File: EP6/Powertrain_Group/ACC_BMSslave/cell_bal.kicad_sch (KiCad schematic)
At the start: 6 parts, among them IC13 NX2301P,215

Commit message: ACC_BMSslave pcb priliminary layout
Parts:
- D13: footprint LED_SMD:LED_0805_2012Metric -> LED_SMD:LED_0603_1608Metric
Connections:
- net CT-: now also D13.1 (K); no longer R103.2
- net at R103.1: now also IC13.3 (D), R104.2, R105.2; no longer D13.1 (K)
- new net: D13.2 (A), R103.2
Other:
- moved on the sheet: D13, R103
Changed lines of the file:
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@@
 	(wire
 		(pts
-			(xy 87.63 76.2) (xy 87.63 77.47)
+			(xy 87.63 73.66) (xy 87.63 74.93)
 		)
 		(stroke
@@
 	(symbol
 		(lib_id "Device:R_Small")
-		(at 87.63 80.01 0)
+		(at 87.63 71.12 0)
 		(unit 1)
 		(exclude_from_sim no)
@@
 		(fields_autoplaced yes)
 		(property "Reference" "R103"
-			(at 90.17 78.7399 0)
+			(at 90.17 69.8499 0)
 			(effects
 				(font
@@
 		)
 		(property "Value" "510"
-			(at 90.17 81.2799 0)
+			(at 90.17 72.3899 0)
 			(effects
 				(font
@@
 		)
 		(property "Footprint" "Resistor_SMD:R_0402_1005Metric"
-			(at 87.63 80.01 0)
+			(at 87.63 71.12 0)
 			(effects
 				(font
@@
 		)
 		(property "Datasheet" "~"
-			(at 87.63 80.01 0)
+			(at 87.63 71.12 0)
 			(effects
 				(font
@@
 		)
 		(property "Description" "Resistor, small symbol"
-			(at 87.63 80.01 0)
+			(at 87.63 71.12 0)
 			(effects
 				(font
@@
 	(symbol
 		(lib_id "Device:LED")
-		(at 87.63 72.39 90)
+		(at 87.63 78.74 90)
 		(unit 1)
 		(exclude_from_sim no)
@@
 		(fields_autoplaced yes)
 		(property "Reference" "D13"
-			(at 91.44 72.7074 90)
+			(at 91.44 79.0574 90)
 			(effects
 				(font
@@
 		)
 		(property "Value" "RED"
-			(at 91.44 75.2474 90)
+			(at 91.44 81.5974 90)
 			(effects
 				(font
@@
 			)
 		)
-		(property "Footprint" "LED_SMD:LED_0805_2012Metric"
-			(at 87.63 72.39 0)
+		(property "Footprint" "LED_SMD:LED_0603_1608Metric"
+			(at 87.63 78.74 0)
 			(effects
 				(font
@@
 		)
 		(property "Datasheet" "~"
-			(at 87.63 72.39 0)
+			(at 87.63 78.74 0)
 			(effects
 				(font
@@
 		)
 		(property "Description" "Light emitting diode"
-			(at 87.63 72.39 0)
-			(effects
-				(font
+			(at 87.63 78.74 0)
+			(effects
+				(font

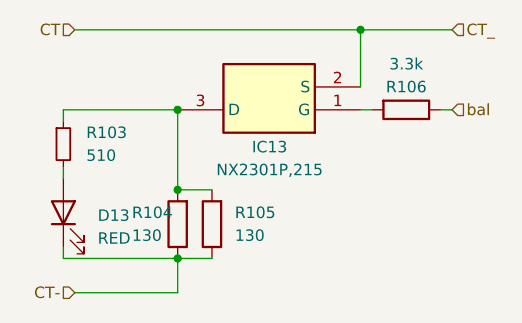
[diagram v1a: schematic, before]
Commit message: ACC_BMSslave changed balancing current
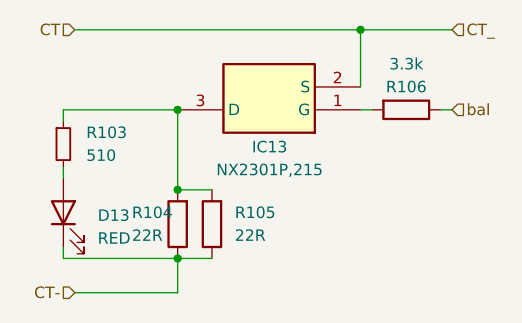
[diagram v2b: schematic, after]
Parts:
- R104, R105: value 130 -> 22R
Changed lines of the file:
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@@
 			)
 		)
-		(property "Value" "130"
+		(property "Value" "22R"
 			(at 95.25 81.28 0)
 			(effects
@@
 			)
 		)
-		(property "Value" "130"
+		(property "Value" "22R"
 			(at 106.68 81.28 0)
 			(effects

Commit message: [BMSslave] snapshot
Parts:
- renumbered D13 to D12, R103 to R105, R104 to R106, R105 to R107, R106 to R108

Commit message: [BMSslave] snapshot
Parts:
- R55: renamed from R108; footprint Resistor_SMD:R_0603_1608Metric -> Resistor_SMD:R_0402_1005Metric
- renumbered D12 to D2, IC13 to IC3, R105 to R52, R106 to R53, R107 to R54

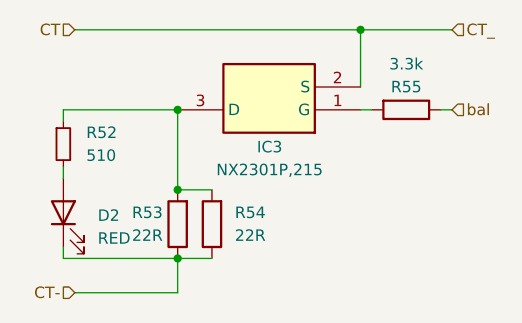
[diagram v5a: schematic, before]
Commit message: update ACC_BMSslave to V3.1
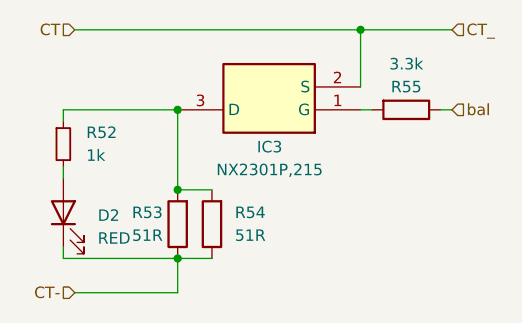
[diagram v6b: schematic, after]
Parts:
- R52: value 510 -> 1k
- R53, R54: value 22R -> 51R
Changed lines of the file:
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@@
 			)
 		)
-		(property "Value" "510"
+		(property "Value" "1k"
 			(at 90.17 72.3899 0)
 			(effects
@@
 			)
 		)
-		(property "Value" "22R"
+		(property "Value" "51R"
 			(at 95.25 81.28 0)
 			(effects
@@
 			)
 		)
-		(property "Value" "22R"
+		(property "Value" "51R"
 			(at 106.68 81.28 0)
 			(effects
